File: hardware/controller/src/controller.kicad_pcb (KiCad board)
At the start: 2 copper layers, 57.9 x 30.7 mm, 41 parts, among them J1 Column Connector, J2 Row Connector, J3 12V DC Barrel Jack, J4 USB C, SW1 RESET, SW2 BOOT, U1 ESP32-S3-WROOM-1, U2 XL1509-5.0, U3 XC6206P332MR, U4 MT9700

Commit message: Documentation Updates
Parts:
- added J5: Conn_01x02, Connector_AMASS:AMASS_XT30U-M_1x02_P5.0mm_Vertical, F.Cu at (3.12, 3.12)

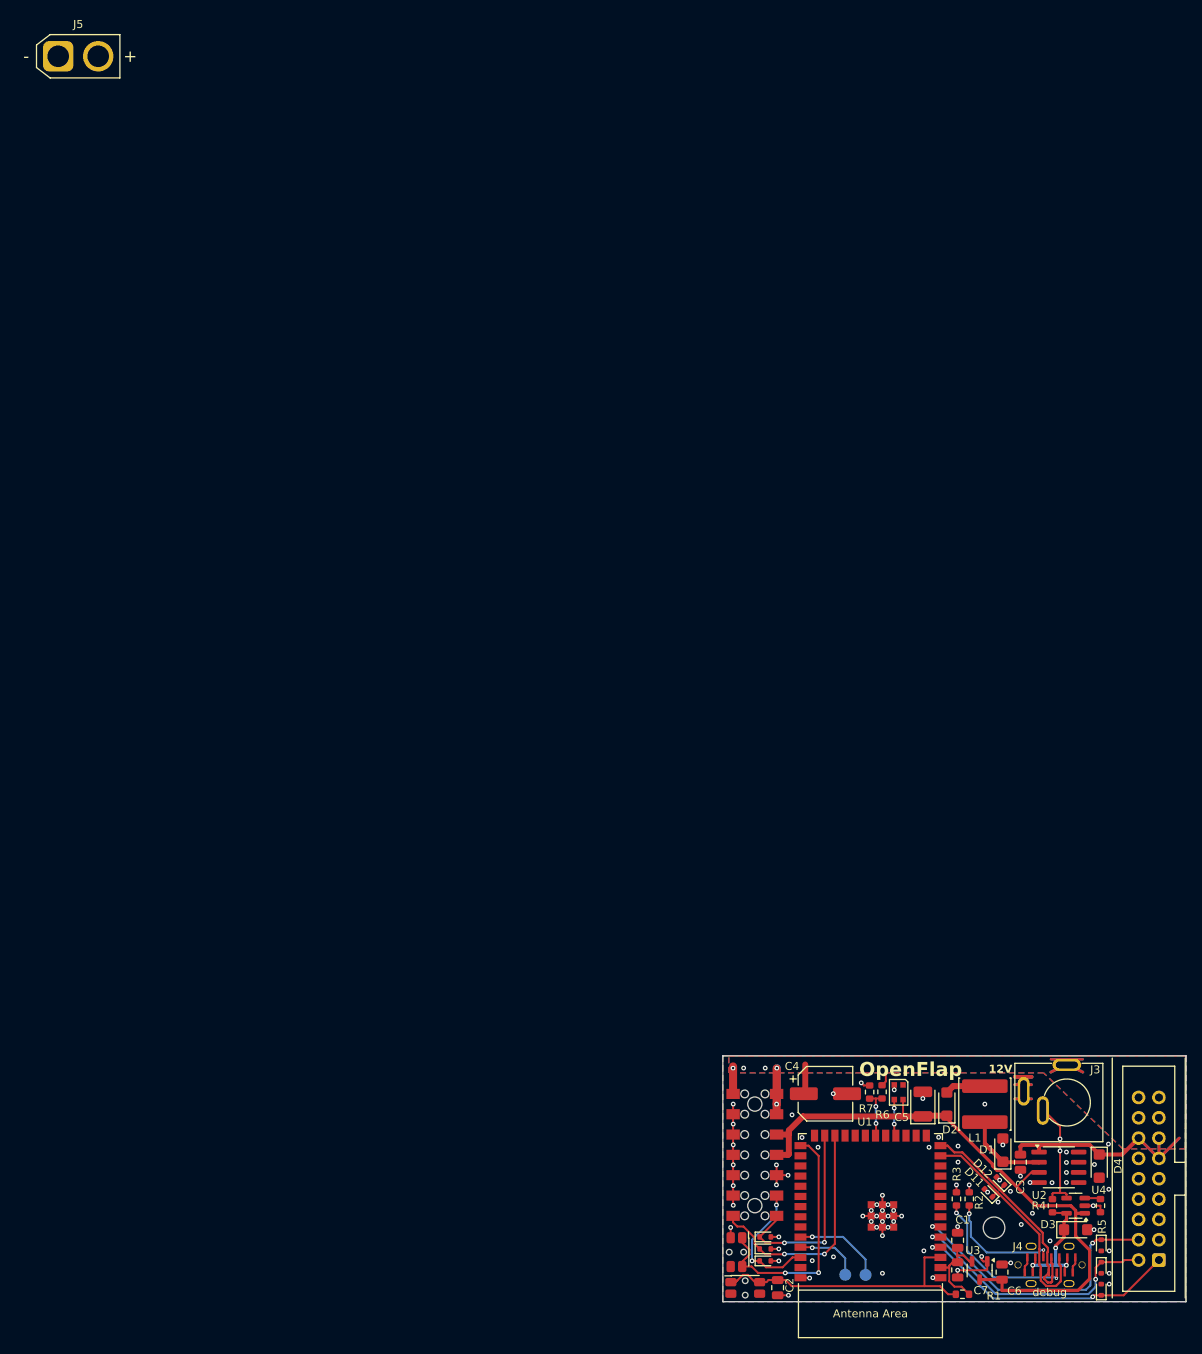
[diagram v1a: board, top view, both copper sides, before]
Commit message: Change barel jack for XT30 connector and bump LDO to 600mA, remove usb power switch  in favor of diode.
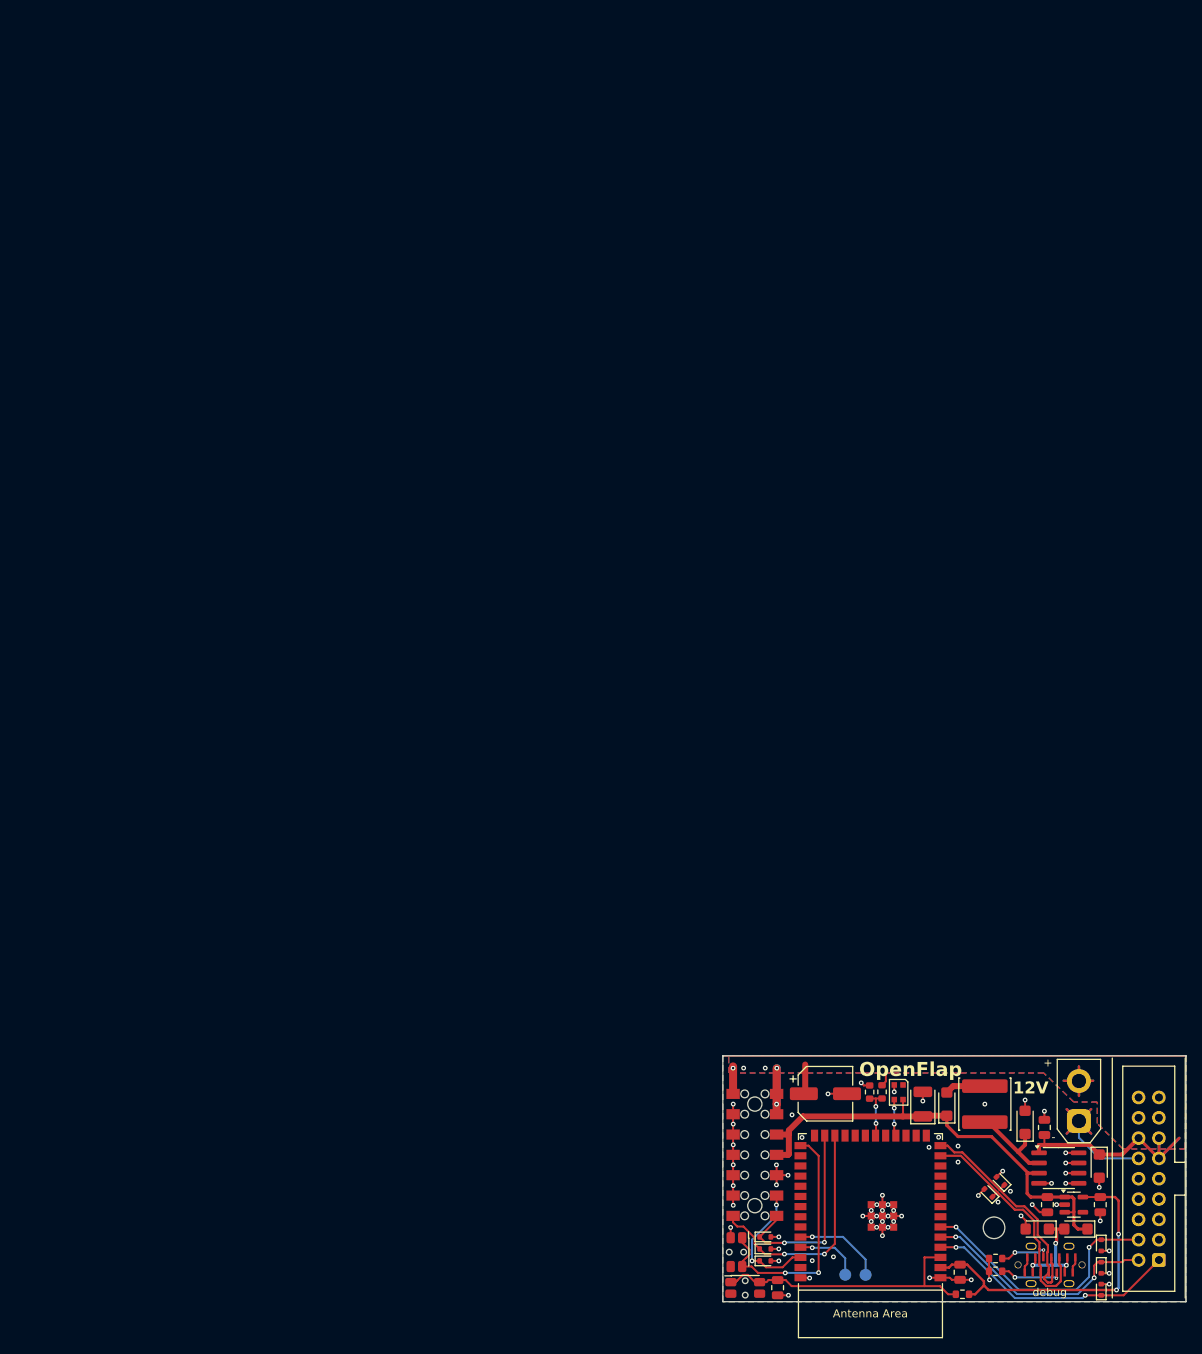
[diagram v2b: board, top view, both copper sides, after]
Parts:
- removed J3: 12V DC Barrel Jack, DC-jack-connector:DC-012A-25A
- removed R4, R5: 10K, Resistor_SMD:R_0603_1608Metric
- removed U4: MT9700, Package_TO_SOT_SMD:SOT-23-5
- added D13: K24, Diode_SMD:D_SMF, F.Cu at (130.3, 149.7)
- J5: value Conn_01x02 -> XT30UPB; footprint Connector_AMASS:AMASS_XT30U-M_1x02_P5.0mm_Vertical -> Connector_AMASS:AMASS_XT30UPB-M_1x02_P5.0mm_Vertical
- U3: value XC6206P332MR -> AP2112K-3.3; footprint Package_TO_SOT_SMD:SOT-23-3 -> Package_TO_SOT_SMD:SOT-23-5
- moved J5 184.4 mm to (130.7, 136.2), turned to 90 degrees
- moved C7 19.6 mm to (133.4, 146.7)
- moved U3 14.4 mm to (130.1, 146.7), turned to 0 degrees
- moved R3 10.3 mm to (120.3, 155.0), turned to 180 degrees
- moved C6 10.2 mm to (126.8, 146.7), turned to -90 degrees
- moved R2 8.15 mm to (120.3, 153.4), turned to 180 degrees
- moved C3 5.28 mm to (126.4, 137.0), turned to 90 degrees
- moved D3 4.79 mm to (125.5, 149.7), turned to 180 degrees
- moved D1 4.45 mm to (124.0, 136.4)
- moved C1 4.01 mm to (115.9, 155.1), turned to -90 degrees
- moved U2 0.09 mm to (128.2, 142.1)
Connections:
- J5 pad 1: unconnected-(J5-Pin_1-Pad1) -> GND
- J5 pad 2: unconnected-(J5-Pin_2-Pad2) -> +12V
- U3 pad 1: GND -> +5V
- U3 pad 2: +3V3 -> GND
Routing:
- net +3V3: track 11.7 -> 42.0 mm, vias 0 -> 2
- net GND: track 55.5 -> 79.3 mm, vias 77 -> 66
- net +5V: track 80.0 -> 58.8 mm
- net /DC_JACK_SW: track 14.4 -> 0.00 mm, vias 2 -> 0
- net Net-(J4-CC2): track 19.7 -> 8.06 mm
- net Net-(J4-CC1): track 15.0 -> 6.55 mm
- net /ROW START: track 35.2 -> 32.4 mm
- net /UART1_TX_A: track 32.9 -> 30.4 mm
- net +12V: track 33.2 -> 31.0 mm
- net /UART1_RX_A: track 33.9 -> 31.9 mm
- net VBUS: track 17.2 -> 15.2 mm
- net Net-(U4-SET): track 1.97 -> 0.00 mm
- net Net-(D1-K): track 13.8 -> 13.0 mm
- net /USB_D+: track 28.9 -> 29.5 mm
- net /USB_D-: track 29.2 -> 29.8 mm
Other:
- board text added: "+"
- board text added: "-"

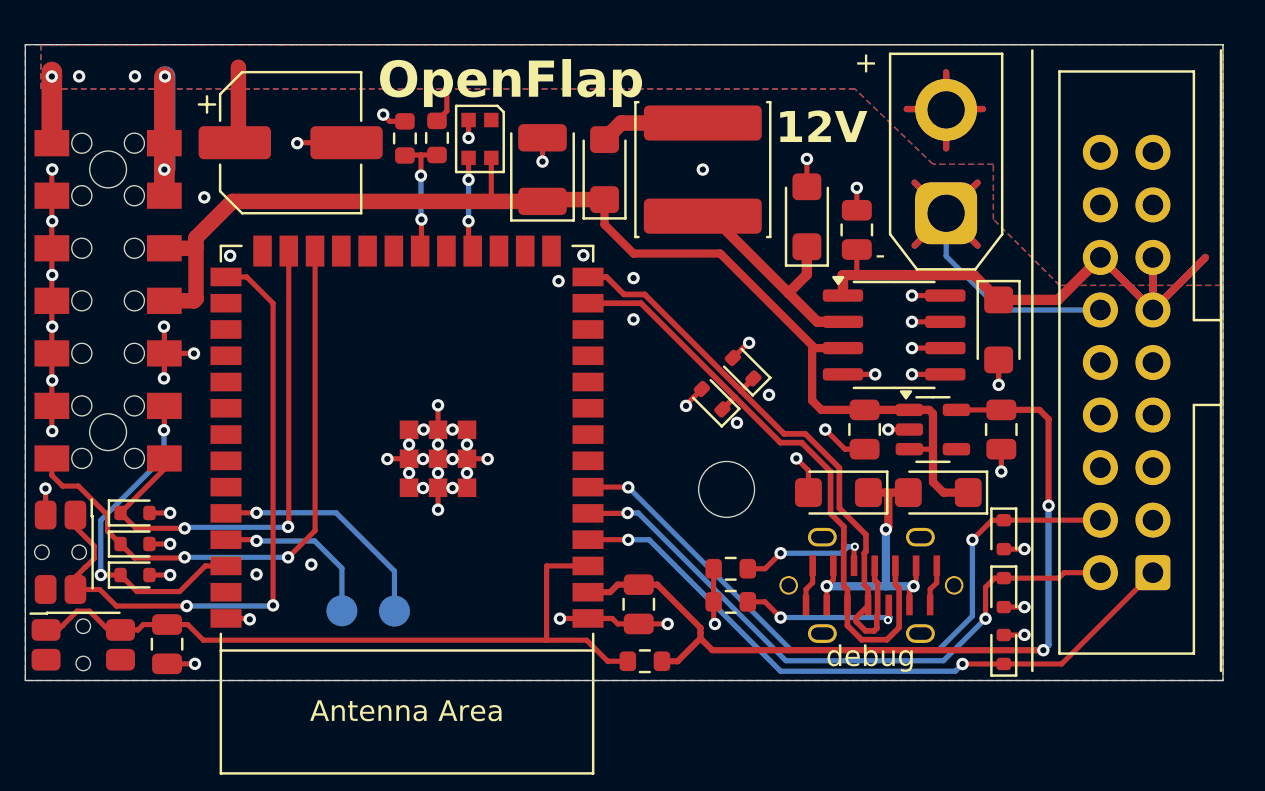
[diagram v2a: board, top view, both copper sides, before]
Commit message: Add test points to pcb's
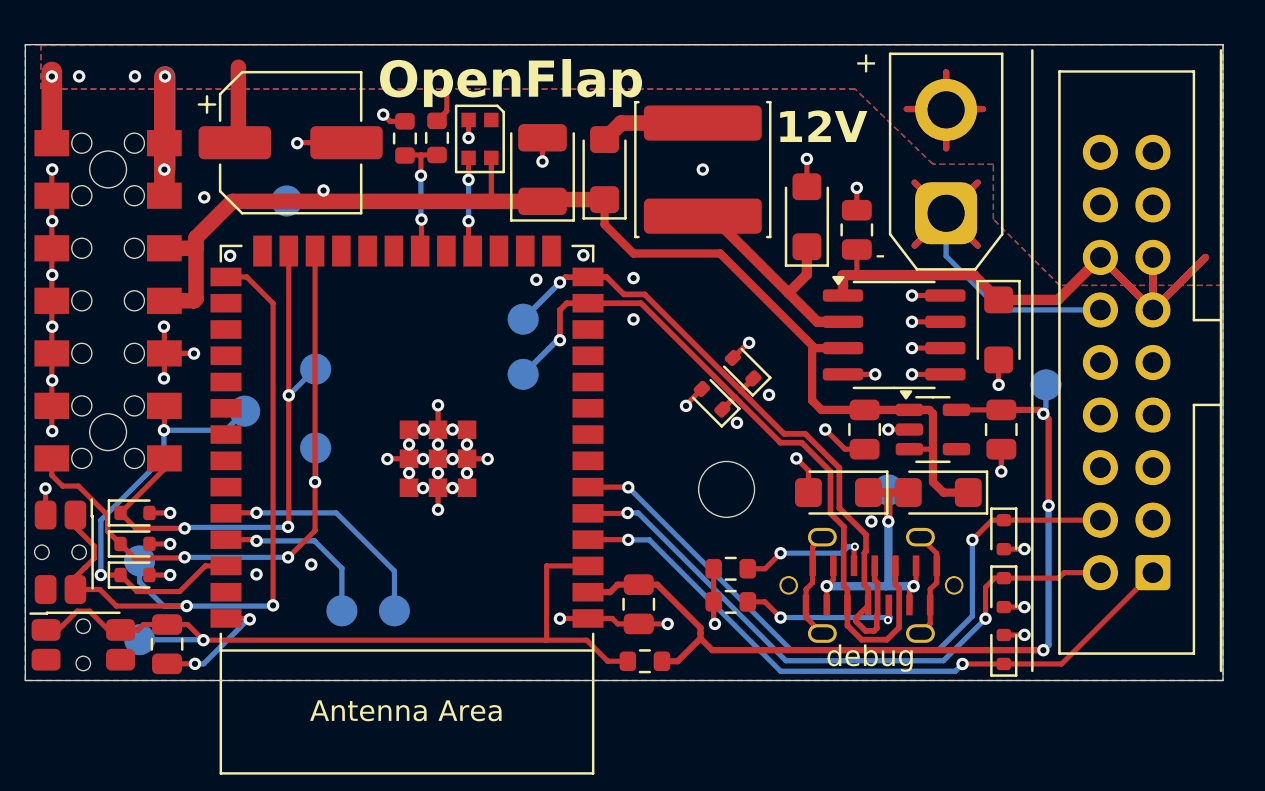
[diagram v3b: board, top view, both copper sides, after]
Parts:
- removed RX0: TestPoint, TestPoint:TestPoint_Pad_D1.5mm
- added TP1: TestPoint, TestPoint:TestPoint_Pad_D1.5mm, B.Cu at (104.0, 155.4)
- added TP10: TestPoint, TestPoint:TestPoint_Pad_D1.5mm, B.Cu at (100.2, 143.8)
- added TP11: TestPoint, TestPoint:TestPoint_Pad_D1.5mm, B.Cu at (91.7, 156.8)
- added TP2: TestPoint, TestPoint:TestPoint_Pad_D1.5mm, B.Cu at (110.3, 141.3)
- added TP3: TestPoint, TestPoint:TestPoint_Pad_D1.5mm, B.Cu at (110.3, 144.0)
- added TP4: TestPoint, TestPoint:TestPoint_Pad_D1.5mm, B.Cu at (91.7, 153.0)
- added TP5: TestPoint, TestPoint:TestPoint_Pad_D1.5mm, B.Cu at (96.8, 145.8)
- added TP6: TestPoint, TestPoint:TestPoint_Pad_D1.5mm, B.Cu at (98.8, 135.6)
- added TP7: TestPoint, TestPoint:TestPoint_Pad_D1.5mm, B.Cu at (127.9, 149.6)
- added TP8: TestPoint, TestPoint:TestPoint_Pad_D1.5mm, B.Cu at (135.5, 144.5)
- added TP9: TestPoint, TestPoint:TestPoint_Pad_D1.5mm, B.Cu at (100.2, 147.6)
- renumbered C2 to C1, C4 to C2, C5 to C4, C6 to C5, C7 to C6, C1 to C7, D13 to D1, D9 to D10, D10 to D11, D11 to D12, D12 to D13, D3 to D2, D4 to D3, D1 to D4, D2 to D7, D7 to D8, D8 to D9, J4 to J1, J5 to J2, J1 to J3, J2 to J4, R6 to R4, R7 to R5, SW2 to SW1, SW1 to SW2, TX0 to TP0, U2 to U1, U1 to U2
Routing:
- net GND: track 79.3 -> 89.4 mm, vias 66 -> 67
- net /USB_D-: track 29.8 -> 35.2 mm, vias 0 -> 1
- net /COL START: track 16.5 -> 20.8 mm
- net /USB_D+: track 29.5 -> 33.4 mm, vias 0 -> 1
- net /IO0: track 31.7 -> 35.4 mm
- net /EN: track 35.3 -> 38.4 mm, vias 0 -> 1
- net +5V: track 58.8 -> 61.3 mm, vias 0 -> 1
- net /UART1_RX_B: track 25.4 -> 27.2 mm, vias 2 -> 3
- net /UART1_TX_B: track 29.7 -> 31.4 mm, vias 2 -> 3
- net VBUS: track 15.2 -> 16.7 mm
- net +3V3: track 42.0 -> 43.5 mm, vias 2 -> 3
